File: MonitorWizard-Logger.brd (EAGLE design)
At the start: 125 x 80 mm, 35 parts, among them CON1 MICROSD, IC1 LD117AV33, J1 22-27-2041-04, J2 22-27-2041-04, J3 22-27-2041-04, U1 DHT22, U2 RFM69HW, U3 LTC3531, U4-NRF24L01 NRF24L01+-PCB-AERIAL, U6 ATMEGA328P-PU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

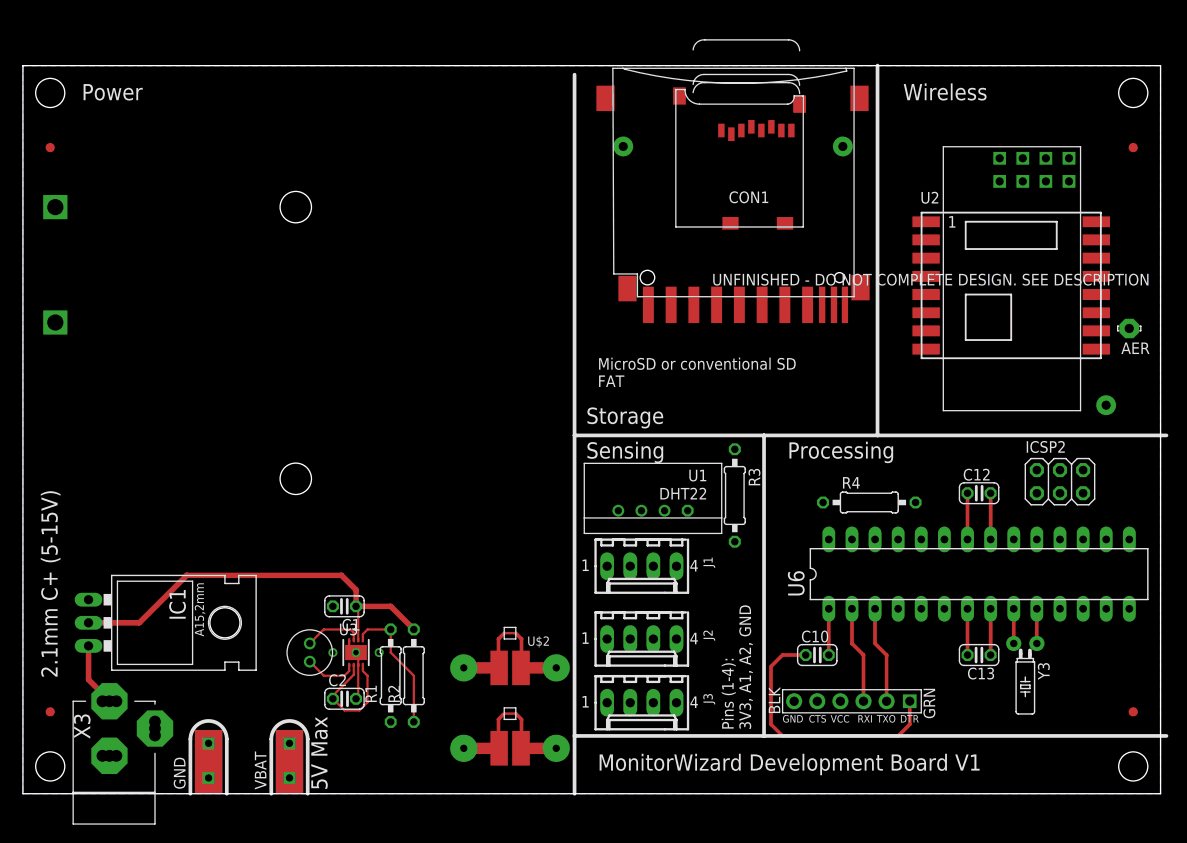
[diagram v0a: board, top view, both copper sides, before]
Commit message: Add decoupling capacitors, begin to route board.
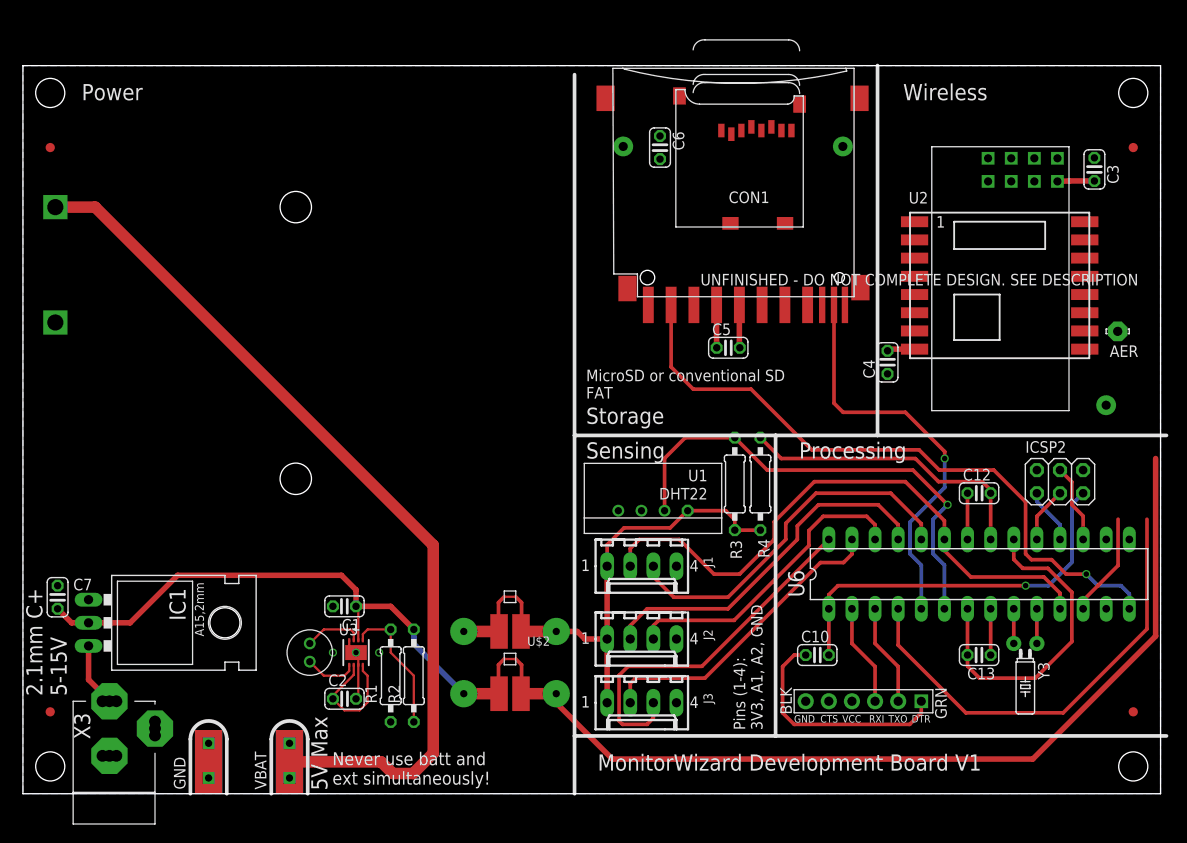
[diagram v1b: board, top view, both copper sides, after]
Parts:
- added C3, C4, C5, C6, C7: 0.1u, rcl:C025-024X044
- moved R4 12.1 mm to (81.0, 34.0), turned to 90 degrees
- moved RF_CURRENT 6.00 mm to (53.5, 11.0)
- moved SENSOR_CURRENT 4.00 mm to (53.5, 17.8)
- moved AER 1.31 mm to (120.3, 50.8)
- moved U2 1.27 mm to (107.3, 55.9)
- moved JP1 1.27 mm to (92.4, 10.2)
- moved R3 1.27 mm to (78.2, 34.0)
- moved U4-NRF24L01 1.27 mm to (109.9, 68.5)
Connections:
- net EXT_SENSOR_POWER renamed SENSOR_POWER
- removed net +5V: ICSP2.2
- removed net DHT22_3V3: R3.2, U1.VDD, U6.13
- removed net EXT_SENSOR_3V3: J1.1, J2.1, J3.1, R4.1, SENSOR_CURRENT.P$2
- removed net RFMODULE_MISC2: U6.4
- new net SENSOR_3V3: J1.1, J2.1, J3.1, R3.2, R4.1, SENSOR_CURRENT.P$2, U1.VDD
- net 3V3: now also C5.2, C6.2, C7.2
- net GND: now also C3.1, C4.1, C5.1, C6.1, C7.1
- net RFMODULE_3V3: now also C3.2, C4.2
- net RFMODULE_MISC2_INT: now also U6.4
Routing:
- net RFMODULE_3V3: track 0.00 -> 101.6 mm
- net VBAT: track 13.8 -> 110.8 mm
- net SD_CS: track 0.00 -> 72.5 mm, vias 0 -> 1
- net EXT_ANALOG_0_TIM: track 0.00 -> 65.2 mm
- net DHT22_DATA: track 0.00 -> 53.4 mm, vias 0 -> 1
- net RFMODULE_MISC2_INT: track 0.00 -> 50.3 mm
- net 3V3: track 50.5 -> 99.0 mm
- net SD_DETECT: track 0.00 -> 44.5 mm, vias 0 -> 1
- net SENSOR_3V3: track 0.00 -> 43.2 mm
- net EXT_ANALOG_1: track 0.00 -> 40.4 mm
- net EXT_ANALOG_5: track 0.00 -> 40.1 mm
- net EXT_ANALOG_2: track 0.00 -> 39.8 mm
- net RESET1: track 5.08 -> 42.9 mm, vias 0 -> 1
- net EXT_ANALOG_4: track 0.00 -> 34.0 mm
- net EXT_ANALOG_3: track 0.00 -> 33.8 mm
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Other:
- board text added: "2.1mm C+ 5-15V"
- board text added: "Never use batt and ext simultaneously!"
- board text removed: "2.1mm C+ (5-15V)"

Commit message: Route most of layout - just have to route (and terminate?) the SPI bus now.
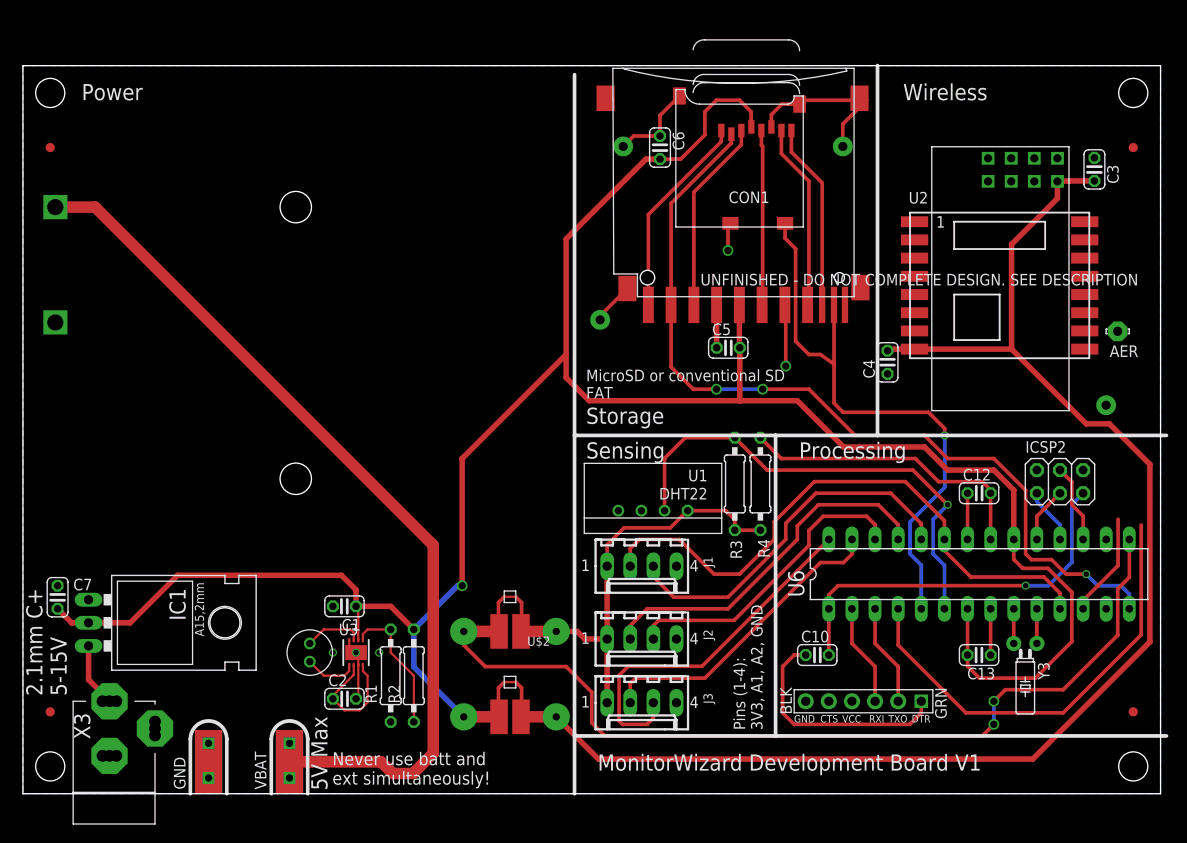
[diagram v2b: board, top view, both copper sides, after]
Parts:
- moved RF_CURRENT 2.54 mm to (53.5, 8.45)
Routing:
- net 3V3: track 99.0 -> 250.0 mm, vias 0 -> 1
- net SENSOR_POWER: track 0.44 -> 97.0 mm, vias 0 -> 2
- net RFMODULE_3V3: track 101.6 -> 150.7 mm
- net GND: track 22.0 -> 64.9 mm, vias 6 -> 9
- net SD_DAT2: track 0.00 -> 22.5 mm
- net SD_CS: track 72.5 -> 94.7 mm, vias 1 -> 3
- net MOSI1: track 8.67 -> 30.0 mm
- net MISO1: track 6.13 -> 27.3 mm
- net SD_DAT1: track 0.00 -> 20.6 mm
- net SD_DETECT: track 44.5 -> 64.6 mm
- net SCK1: track 6.13 -> 25.4 mm
- net RFMODULE_MISC2_INT: track 50.3 -> 49.4 mm

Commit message: Route remaining wires. Still needs the following: Confirm SD card current draw (idle, writing) - is a FET required to power the SD card down? Impedance matching SPI lines / SPI routing improvements? Full DRC check / capabilities of board house around power circuitry Any other improvements / errors before sending off?
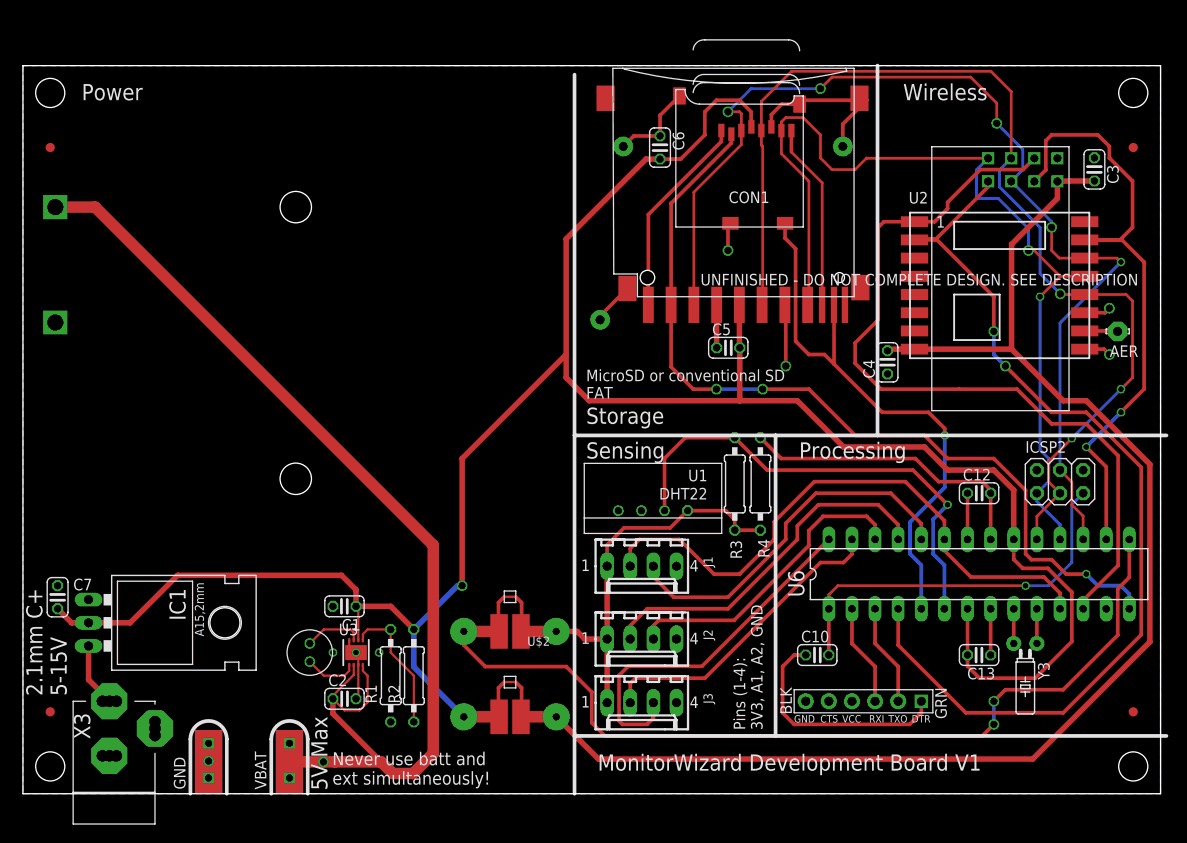
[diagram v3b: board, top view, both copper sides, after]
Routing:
- net SCK1: track 25.4 -> 117.5 mm, vias 0 -> 3
- net MOSI1: track 30.0 -> 119.2 mm, vias 0 -> 5
- net RFMODULE_MISC1: track 11.4 -> 88.2 mm
- net MISO1: track 27.3 -> 103.1 mm, vias 0 -> 2
- net RFMODULE_CS: track 0.00 -> 70.1 mm, vias 0 -> 2
- net RFMODULE_MISC2_INT: track 49.4 -> 105.9 mm, vias 0 -> 2
- net VBAT: track 110.8 -> 123.7 mm, vias 0 -> 1
- net GND: track 64.9 -> 71.8 mm, vias 9 -> 11
- net N$9: track 0.00 -> 3.64 mm
- net SD_DETECT: track 64.6 -> 62.2 mm

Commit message: Fix some DRC errors, tidy silkscreen, improve grounding.
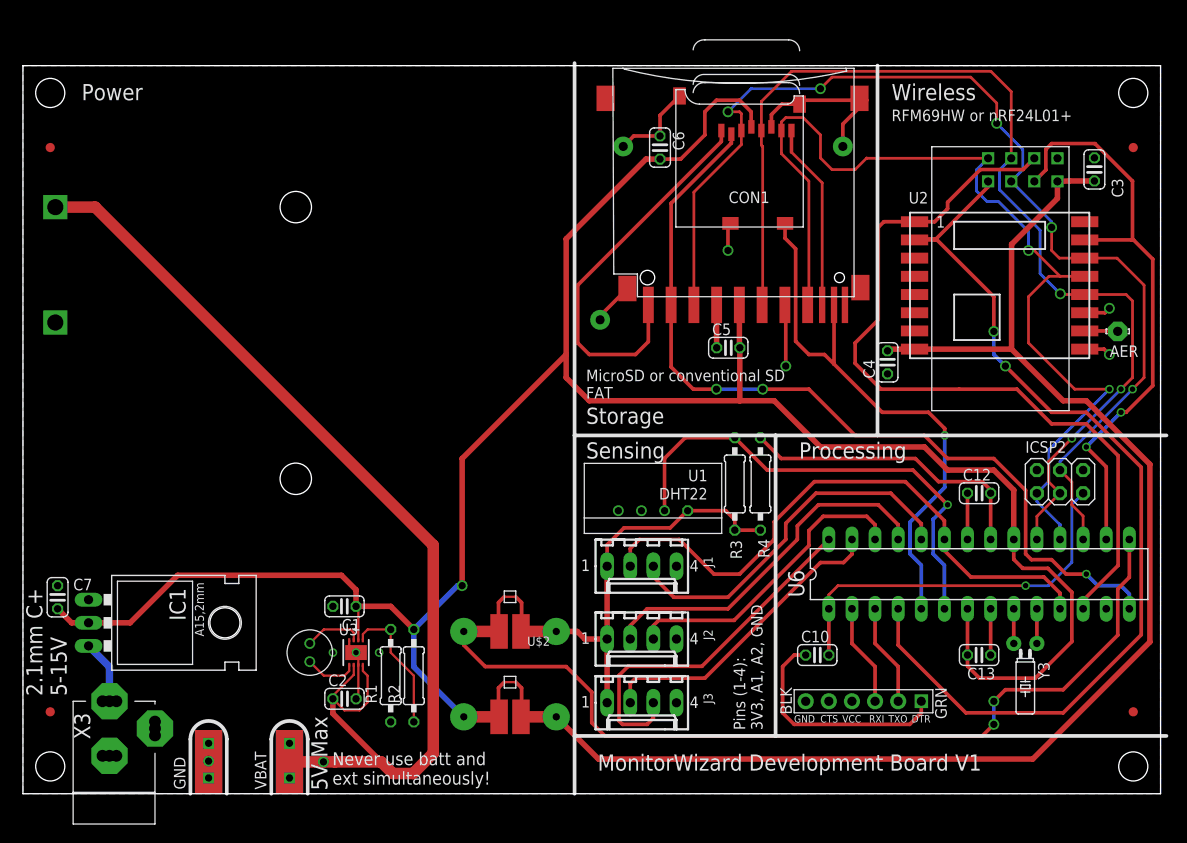
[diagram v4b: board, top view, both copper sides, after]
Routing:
- net SD_DAT2: track 22.5 -> 42.8 mm
- net MISO1: track 103.1 -> 111.9 mm
- net RFMODULE_CS: track 70.1 -> 65.5 mm
- net MOSI1: track 119.2 -> 121.3 mm
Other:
- board text added: "RFM69HW or nRF24L01+"

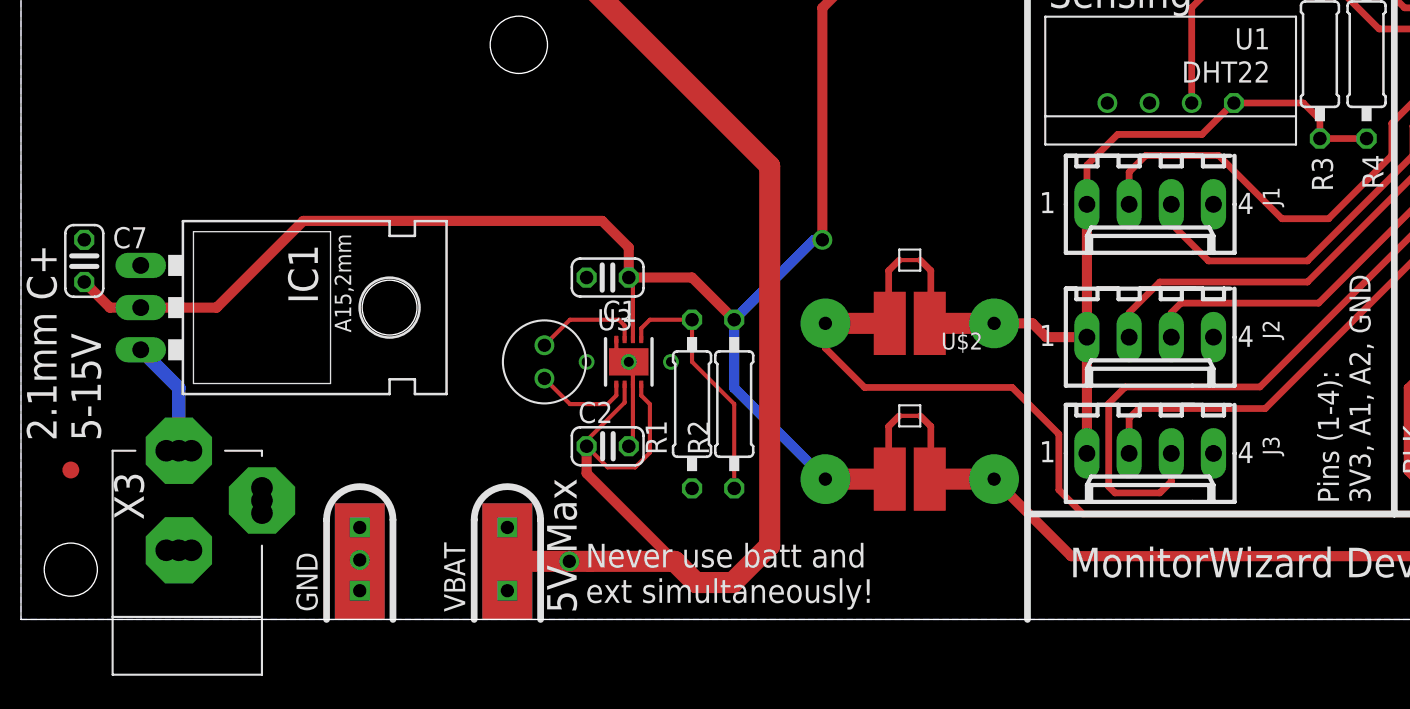
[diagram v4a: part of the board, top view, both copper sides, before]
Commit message: More silkscreen fixes, move power jack to make more room for screw, tweak spacing of sensor connectors.
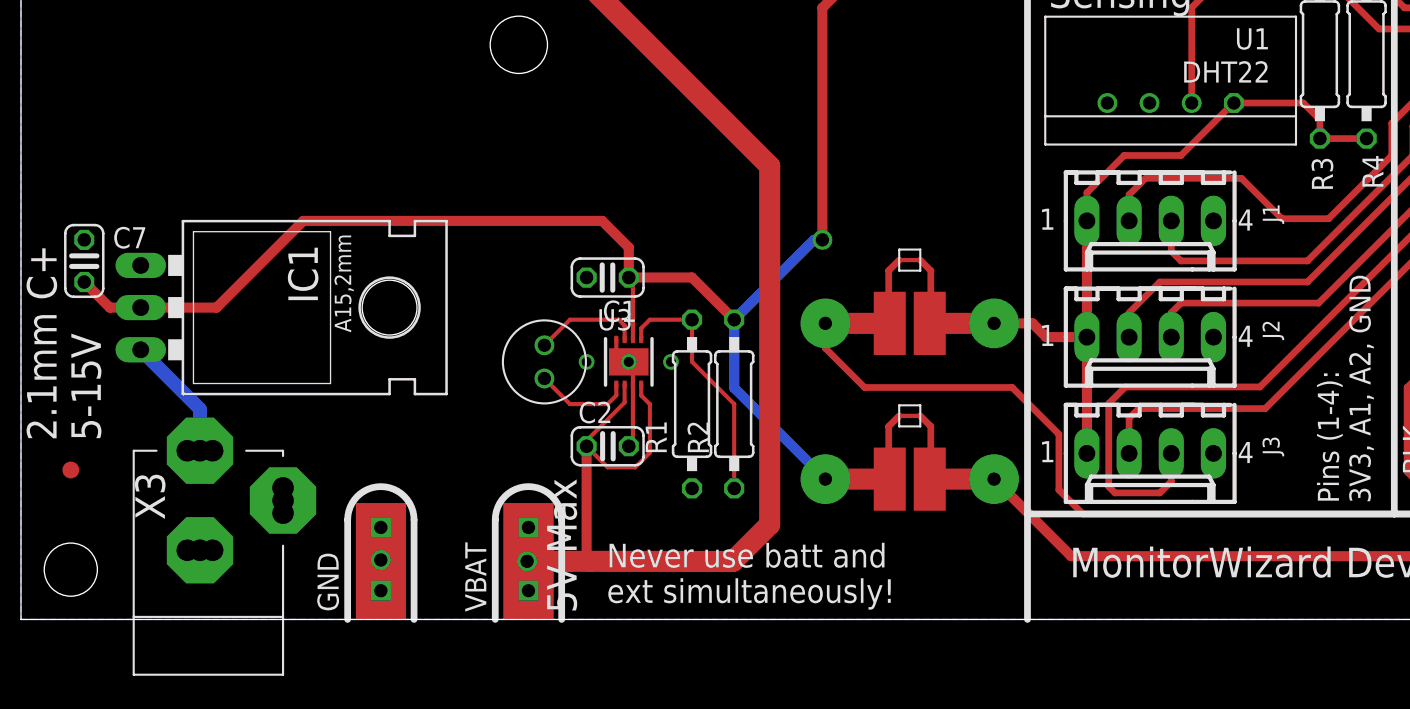
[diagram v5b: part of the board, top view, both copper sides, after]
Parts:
- moved GND 1.27 mm to (21.7, 0.00)
- moved VBAT 1.27 mm to (30.6, 0.00)
- moved X3 1.27 mm to (10.7, 3.81)
- moved J1 1.00 mm to (68.0, 24.0)
- renumbered RF_CURRENT to I_RF, SENSOR_CURRENT to I_SENSE
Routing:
- net VBAT: track 123.7 -> 115.0 mm
- net SENSOR_3V3: track 43.2 -> 42.3 mm
- net EXT_ANALOG_0_TIM: track 65.2 -> 64.3 mm
- net VBJ: track 7.03 -> 7.56 mm

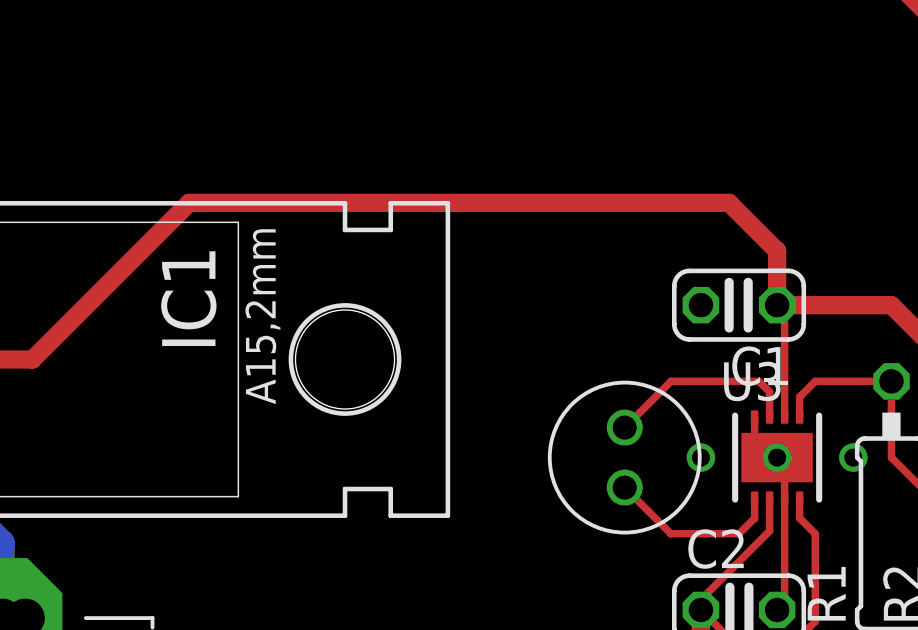
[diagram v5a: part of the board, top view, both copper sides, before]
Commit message: Add electrolytic filter capacitor.
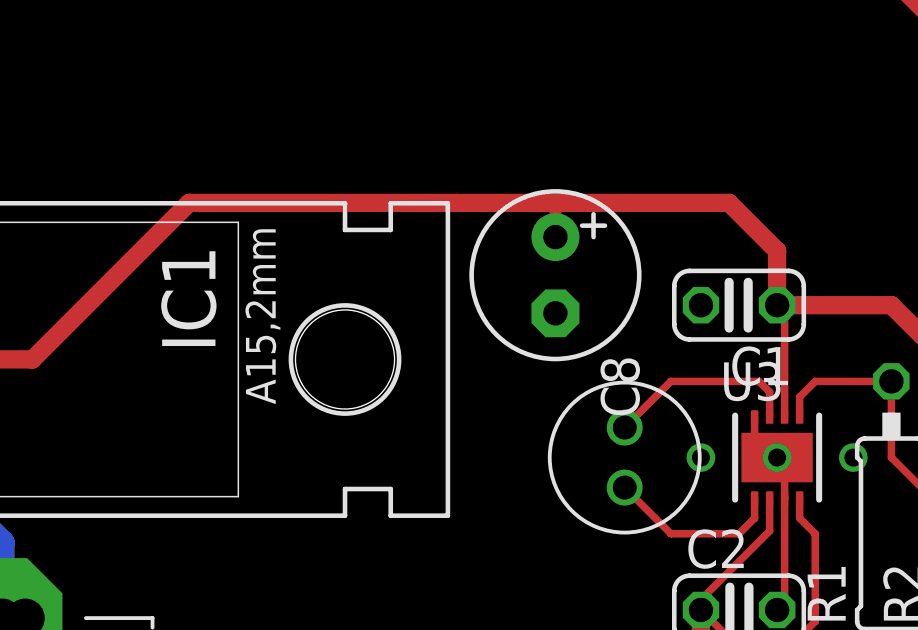
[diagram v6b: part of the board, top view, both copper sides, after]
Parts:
- added C8: (no value), rcl:E2,5-6
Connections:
- net 3V3: now also C8.+
- net GND: now also C8.-
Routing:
- net 3V3: track 250.0 -> 251.2 mm
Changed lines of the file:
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@@
 <attribute name="VALUE" x="5.5245" y="24.003" size="1.27" layer="27" ratio="10"/>
 </element>
+<element name="C8" library="rcl" package="E2,5-6" value="" x="29.21" y="21.59" rot="R270"/>
 </elements>
 <signals>
@@
 <wire x1="21.67" y1="3.5" x2="21.67" y2="3.5814" width="0.3048" layer="1"/>
 <via x="21.67" y="3.5814" extent="1-16" drill="0.8"/>
+<contactref element="C8" pad="-"/>
 </signal>
 <signal name="AREF" class="4">
@@
 <wire x1="7.21" y1="18.78" x2="11.78" y2="18.78" width="0.6096" layer="1"/>
 <wire x1="11.78" y1="18.78" x2="17" y2="24" width="0.6096" layer="1"/>
-<wire x1="17" y1="24" x2="35" y2="24" width="0.6096" layer="1"/>
+<wire x1="17" y1="24" x2="29.21" y2="24" width="0.6096" layer="1"/>
+<wire x1="29.21" y1="24" x2="35" y2="24" width="0.6096" layer="1"/>
 <wire x1="35" y1="24" x2="36.6" y2="22.4" width="0.6096" layer="1"/>
 <wire x1="36.6" y1="22.4" x2="36.6" y2="20.59" width="0.6096" layer="1"/>
@@
 <wire x1="48.26" y1="22.86" x2="47.76" y2="22.86" width="0.6096" layer="16"/>
 <wire x1="47.76" y1="22.86" x2="42.95" y2="18.05" width="0.6096" layer="16"/>
+<contactref element="C8" pad="+"/>
+<wire x1="29.21" y1="22.86" x2="29.21" y2="24" width="0.4064" layer="1"/>
 </signal>
 <signal name="SENSOR_POWER">
